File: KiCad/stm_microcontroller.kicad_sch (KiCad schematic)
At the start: 16 parts, among them SW1 SW_Push, SW2 SW_Push, U4 STM32G0B1CBTx, Y1 8Mhz

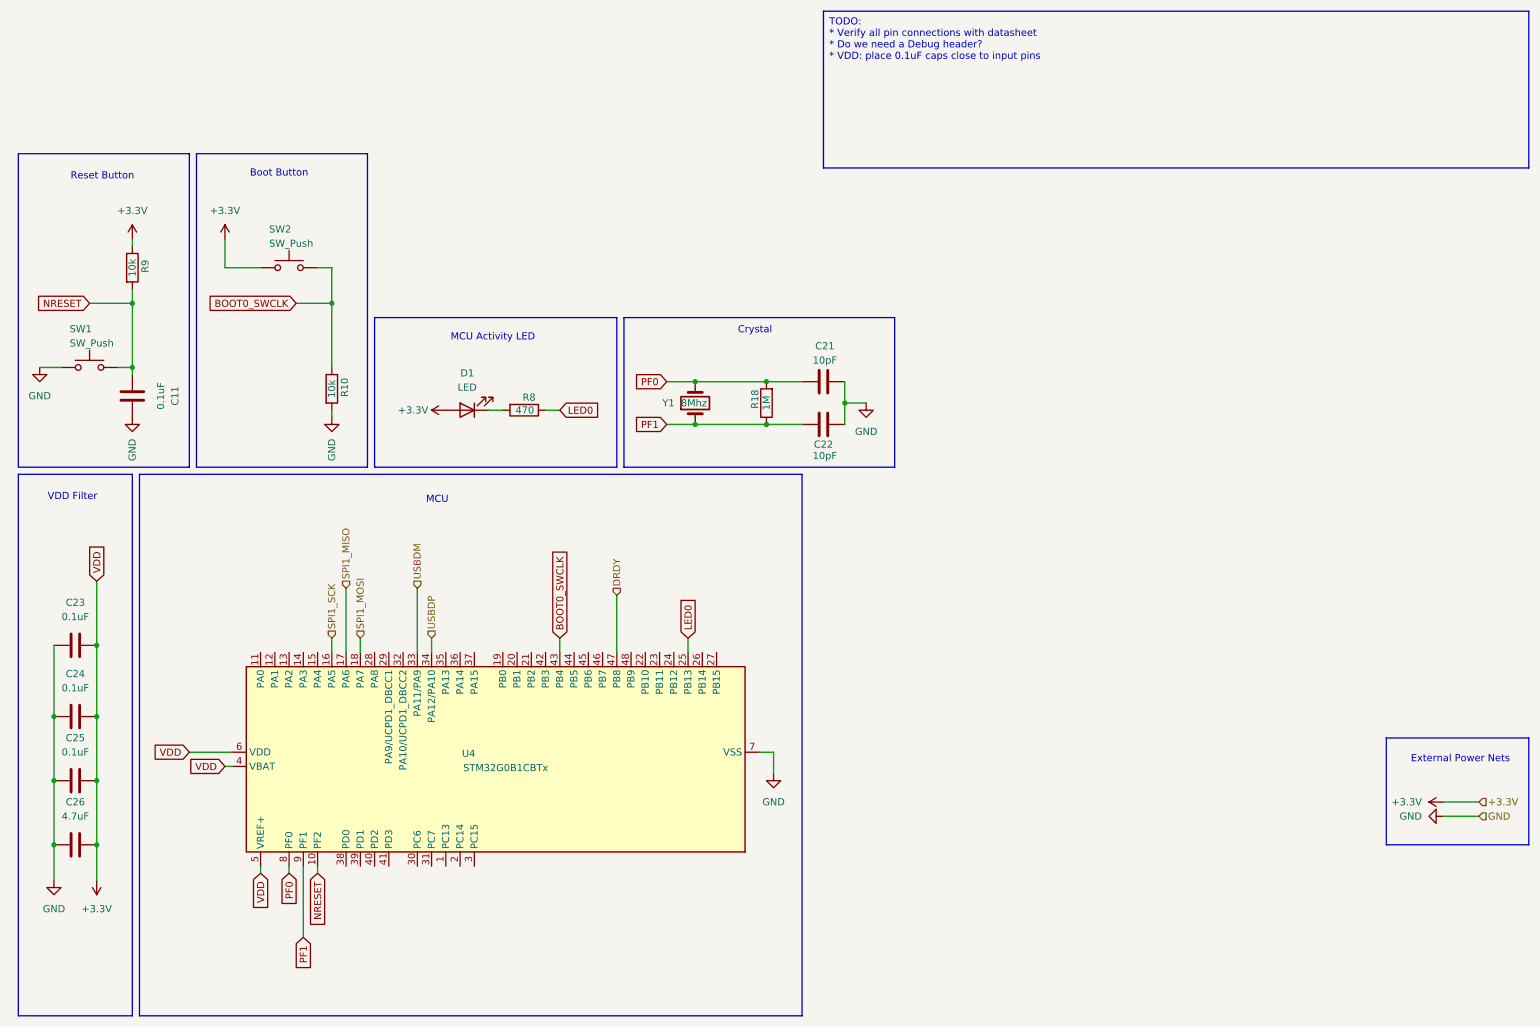
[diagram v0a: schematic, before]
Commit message: Use 12V Power
* Use 12 V Power
* Update to an F103 processor with better compatibility with Katapult
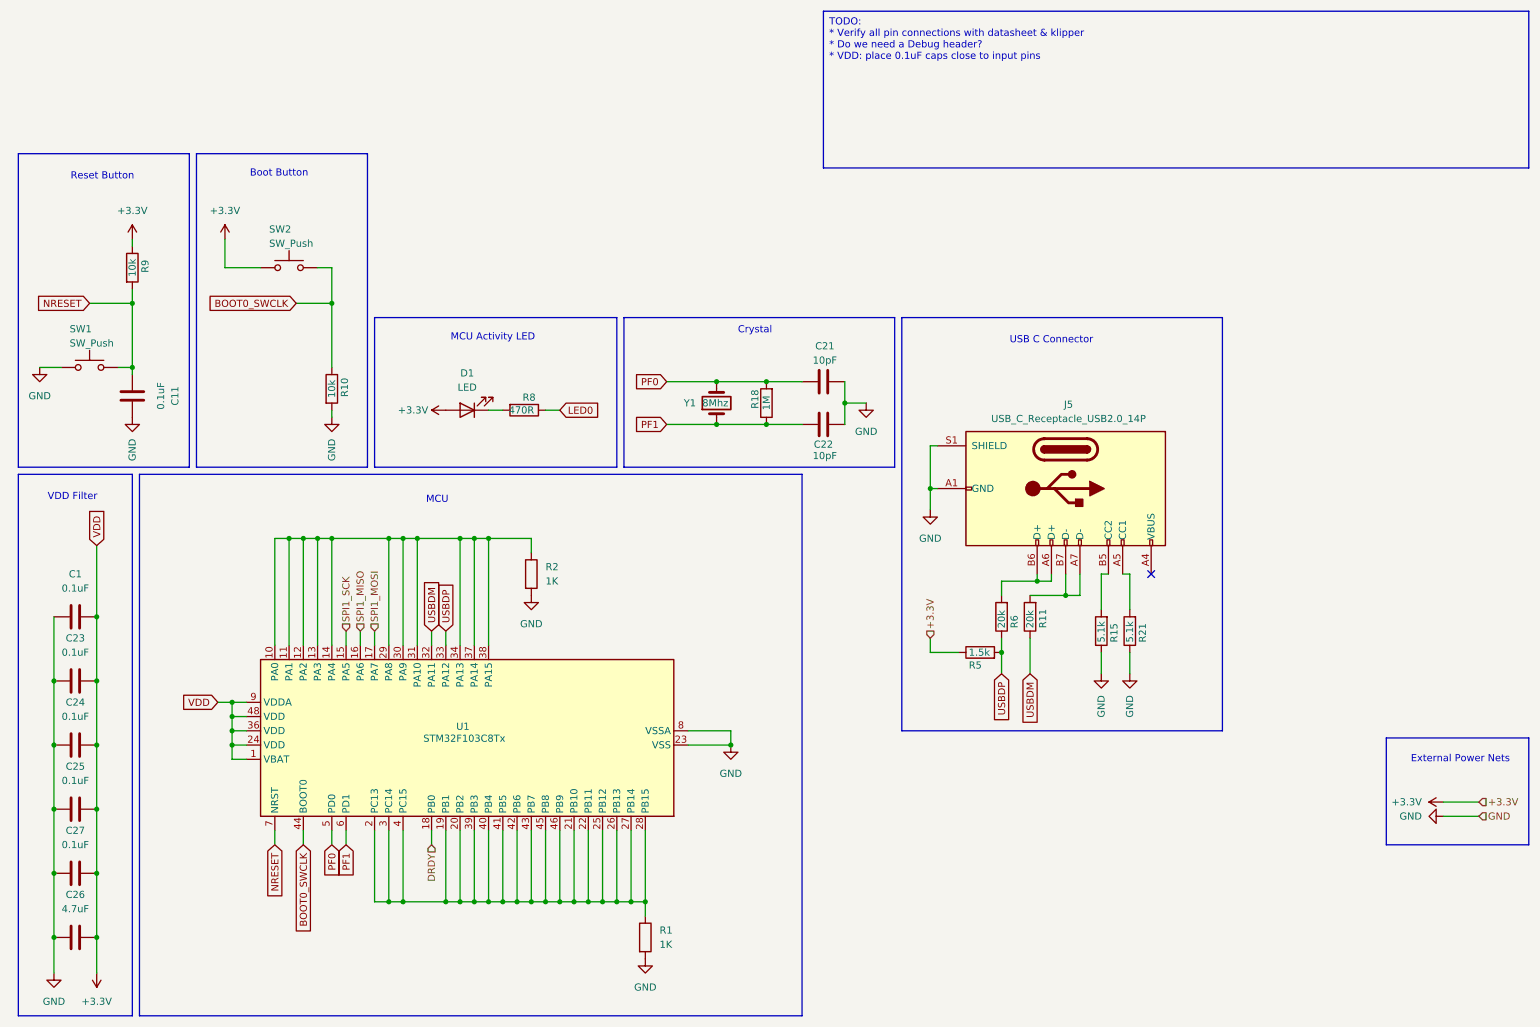
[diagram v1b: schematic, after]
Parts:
- removed U4: STM32G0B1CBTx, Package_QFP:LQFP-48_7x7mm_P0.5mm, symbol MCU_ST_STM32G0:STM32G0B1CBTx
- added C1, C27: 0.1uF, Capacitor_SMD:C_0603_1608Metric_Pad1.08x0.95mm_HandSolder, symbol Device:C
- added J5: USB_C_Receptacle_USB2.0_14P, Connector_USB:USB_C_Receptacle_GCT_USB4110, symbol Connector:USB_C_Receptacle_USB2.0_14P
- added R1, R2: 1K, Resistor_SMD:R_0603_1608Metric_Pad0.98x0.95mm_HandSolder, symbol Device:R
- added R11, R6: 20k, Resistor_SMD:R_0603_1608Metric_Pad0.98x0.95mm_HandSolder, symbol Device:R
- added R15, R21: 5.1k, Resistor_SMD:R_0603_1608Metric_Pad0.98x0.95mm_HandSolder, symbol Device:R
- added R5: 1.5k, Resistor_SMD:R_0603_1608Metric_Pad0.98x0.95mm_HandSolder, symbol Device:R
- added U1: STM32F103C8Tx, Package_QFP:LQFP-48_7x7mm_P0.5mm, symbol MCU_ST_STM32F1:STM32F103C8Tx
- C11, C21, C22, C23, C24, C25, C26: footprint (none) -> Capacitor_SMD:C_0603_1608Metric_Pad1.08x0.95mm_HandSolder
- D1: footprint (none) -> LED_SMD:LED_1206_3216Metric_Pad1.42x1.75mm_HandSolder
- R10, R18, R9: footprint (none) -> Resistor_SMD:R_0603_1608Metric_Pad0.98x0.95mm_HandSolder
- R8: value 470 -> 470R; footprint (none) -> Resistor_SMD:R_0603_1608Metric_Pad0.98x0.95mm_HandSolder
- SW1, SW2: footprint (none) -> Button_Switch_SMD:SW_Push_1P1T_NO_6x6mm_H9.5mm
- Y1: footprint (none) -> Crystal:Crystal_SMD_SeikoEpson_FA238V-4Pin_3.2x2.5mm_HandSoldering
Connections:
- net +3.3V: now also C1.2, C27.2, R5.1, U1.1 (VBAT), U1.24 (VDD), U1.36 (VDD), U1.48 (VDD), U1.9 (VDDA)
- net BOOT0_SWCLK: now also U1.44 (BOOT0)
- net DRDY: now also U1.18 (PB0)
- net GND: now also C1.1, C27.1, J5.A1 (GND), J5.A12 (GND), J5.B1 (GND), J5.B12 (GND), J5.S1 (SHIELD), R1.2, R15.1, R2.2, R21.1, U1.23 (VSS), U1.35 (VSS), U1.47 (VSS), U1.8 (VSSA)
- net NRESET: now also U1.7 (NRST)
- net PF0: now also U1.5 (PD0)
- net PF1: now also U1.6 (PD1)
- net SPI1_MISO: now also U1.16 (PA6)
- net SPI1_MOSI: now also U1.17 (PA7)
- net SPI1_SCK: now also U1.15 (PA5)
- net USBDM: now also R11.1, U1.32 (PA11)
- net USBDP: now also R5.2, R6.1, U1.33 (PA12)
- new net: R2.1, U1.10 (PA0), U1.11 (PA1), U1.12 (PA2), U1.13 (PA3), U1.14 (PA4), U1.29 (PA8), U1.30 (PA9), U1.31 (PA10), U1.34 (PA13), U1.37 (PA14), U1.38 (PA15)
- new net: J5.A4 (VBUS), J5.A9 (VBUS), J5.B4 (VBUS), J5.B9 (VBUS)
- new net: J5.A5 (CC1), R21.2
- new net: J5.A6 (D+), J5.B6 (D+), R6.2
- new net: J5.A7 (D-), J5.B7 (D-), R11.2
- new net: J5.B5 (CC2), R15.2
- new net: R1.1, U1.19 (PB1), U1.2 (PC13), U1.20 (PB2), U1.21 (PB10), U1.22 (PB11), U1.25 (PB12), U1.26 (PB13), U1.27 (PB14), U1.28 (PB15), U1.3 (PC14), U1.39 (PB3), U1.4 (PC15), U1.40 (PB4), U1.41 (PB5), U1.42 (PB6), U1.43 (PB7), U1.45 (PB8), U1.46 (PB9)
- no-connect marks 0 -> 1
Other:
- note added: "USB C Connector"
- moved on the sheet: C23, C24, C25, C26, Y1

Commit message: Update 5V Power Stage
* Update the 5V power stage based on the recommendations from TI.
* Updated standard passive footprint to 0805 hand solder configuration
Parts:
- C1, C11, C21, C22, C23, C24, C25, C26, C27: footprint Capacitor_SMD:C_0603_1608Metric_Pad1.08x0.95mm_HandSolder -> Capacitor_SMD:C_0805_2012Metric_Pad1.18x1.45mm_HandSolder
- R1, R10, R11, R15, R18, R2, R21, R5, R6, R8, R9: footprint Resistor_SMD:R_0603_1608Metric_Pad0.98x0.95mm_HandSolder -> Resistor_SMD:R_0805_2012Metric_Pad1.20x1.40mm_HandSolder
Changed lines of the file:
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@@
 			)
 		)
-		(property "Footprint" "Capacitor_SMD:C_0603_1608Metric_Pad1.08x0.95mm_HandSolder"
+		(property "Footprint" "Capacitor_SMD:C_0805_2012Metric_Pad1.18x1.45mm_HandSolder"
 			(at 27.94 143.8148 0)
 			(effects
@@
 			)
 		)
-		(property "Footprint" "Resistor_SMD:R_0603_1608Metric_Pad0.98x0.95mm_HandSolder"
+		(property "Footprint" "Resistor_SMD:R_0805_2012Metric_Pad1.20x1.40mm_HandSolder"
 			(at 103.632 114.3 90)
 			(effects
@@
 			)
 		)
-		(property "Footprint" "Resistor_SMD:R_0603_1608Metric_Pad0.98x0.95mm_HandSolder"
+		(property "Footprint" "Resistor_SMD:R_0805_2012Metric_Pad1.20x1.40mm_HandSolder"
 			(at 68.072 81.28 90)
 			(effects
@@
 			)
 		)
-		(property "Footprint" "Resistor_SMD:R_0603_1608Metric_Pad0.98x0.95mm_HandSolder"
+		(property "Footprint" "Resistor_SMD:R_0805_2012Metric_Pad1.20x1.40mm_HandSolder"
 			(at 32.512 59.69 90)
 			(effects
@@
 			)
 		)
-		(property "Footprint" "Capacitor_SMD:C_0603_1608Metric_Pad1.08x0.95mm_HandSolder"
+		(property "Footprint" "Capacitor_SMD:C_0805_2012Metric_Pad1.18x1.45mm_HandSolder"
 			(at 27.94 166.6748 0)
 			(effects
@@
 			)
 		)
-		(property "Footprint" "Resistor_SMD:R_0603_1608Metric_Pad0.98x0.95mm_HandSolder"
+		(property "Footprint" "Resistor_SMD:R_0805_2012Metric_Pad1.20x1.40mm_HandSolder"
 			(at 104.14 83.312 90)
 			(effects
@@
 			)
 		)
-		(property "Footprint" "Resistor_SMD:R_0603_1608Metric_Pad0.98x0.95mm_HandSolder"
+		(property "Footprint" "Resistor_SMD:R_0805_2012Metric_Pad1.20x1.40mm_HandSolder"
 			(at 191.008 121.92 90)
 			(effects
@@
 			)
 		)
-		(property "Footprint" "Resistor_SMD:R_0603_1608Metric_Pad0.98x0.95mm_HandSolder"
+		(property "Footprint" "Resistor_SMD:R_0805_2012Metric_Pad1.20x1.40mm_HandSolder"
 			(at 208.788 124.46 90)
 			(effects
@@
 			)
 		)
-		(property "Footprint" "Capacitor_SMD:C_0603_1608Metric_Pad1.08x0.95mm_HandSolder"
+		(property "Footprint" "Capacitor_SMD:C_0805_2012Metric_Pad1.18x1.45mm_HandSolder"
 			(at 27.94 178.1048 0)
 			(effects
@@
 			)
 		)
-		(property "Footprint" "Capacitor_SMD:C_0603_1608Metric_Pad1.08x0.95mm_HandSolder"
+		(property "Footprint" "Capacitor_SMD:C_0805_2012Metric_Pad1.18x1.45mm_HandSolder"
 			(at 153.67 88.5952 0)
 			(effects
@@
 			)
 		)
-		(property "Footprint" "Capacitor_SMD:C_0603_1608Metric_Pad1.08x0.95mm_HandSolder"
+		(property "Footprint" "Capacitor_SMD:C_0805_2012Metric_Pad1.18x1.45mm_HandSolder"
 			(at 161.29 79.0448 0)
 			(effects
@@
 			)
 		)
-		(property "Footprint" "Capacitor_SMD:C_0603_1608Metric_Pad1.08x0.95mm_HandSolder"
+		(property "Footprint" "Capacitor_SMD:C_0805_2012Metric_Pad1.18x1.45mm_HandSolder"
 			(at 27.94 155.2448 0)
 			(effects
@@
 			)
 		)
-		(property "Footprint" "Resistor_SMD:R_0603_1608Metric_Pad0.98x0.95mm_HandSolder"
+		(property "Footprint" "Resistor_SMD:R_0805_2012Metric_Pad1.20x1.40mm_HandSolder"
 			(at 149.098 83.82 90)
 			(effects
@@
 			)
 		)
-		(property "Footprint" "Resistor_SMD:R_0603_1608Metric_Pad0.98x0.95mm_HandSolder"
+		(property "Footprint" "Resistor_SMD:R_0805_2012Metric_Pad1.20x1.40mm_HandSolder"
 			(at 196.088 121.92 90)
 			(effects
@@
 			)
 		)
-		(property "Footprint" "Capacitor_SMD:C_0603_1608Metric_Pad1.08x0.95mm_HandSolder"
+		(property "Footprint" "Capacitor_SMD:C_0805_2012Metric_Pad1.18x1.45mm_HandSolder"
 			(at 27.94 132.3848 0)
 			(effects
@@
 			)
 		)
-		(property "Footprint" "Resistor_SMD:R_0603_1608Metric_Pad0.98x0.95mm_HandSolder"
+		(property "Footprint" "Resistor_SMD:R_0805_2012Metric_Pad1.20x1.40mm_HandSolder"
 			(at 185.42 130.048 90)
 			(effects
@@
 			)
 		)
-		(property "Footprint" "Resistor_SMD:R_0603_1608Metric_Pad0.98x0.95mm_HandSolder"
+		(property "Footprint" "Resistor_SMD:R_0805_2012Metric_Pad1.20x1.40mm_HandSolder"
 			(at 213.868 124.46 90)
 			(effects
@@
 			)
 		)
-		(property "Footprint" "Capacitor_SMD:C_0603_1608Metric_Pad1.08x0.95mm_HandSolder"
+		(property "Footprint" "Capacitor_SMD:C_0805_2012Metric_Pad1.18x1.45mm_HandSolder"
 			(at 27.94 120.9548 0)
 			(effects
@@
 			)
 		)
-		(property "Footprint" "Capacitor_SMD:C_0603_1608Metric_Pad1.08x0.95mm_HandSolder"
+		(property "Footprint" "Capacitor_SMD:C_0805_2012Metric_Pad1.18x1.45mm_HandSolder"
 			(at 35.2552 86.36 0)
 			(effects
@@
 			)
 		)
-		(property "Footprint" "Resistor_SMD:R_0603_1608Metric_Pad0.98x0.95mm_HandSolder"
+		(property "Footprint" "Resistor_SMD:R_0805_2012Metric_Pad1.20x1.40mm_HandSolder"
 			(at 123.952 179.07 90)
 			(effects

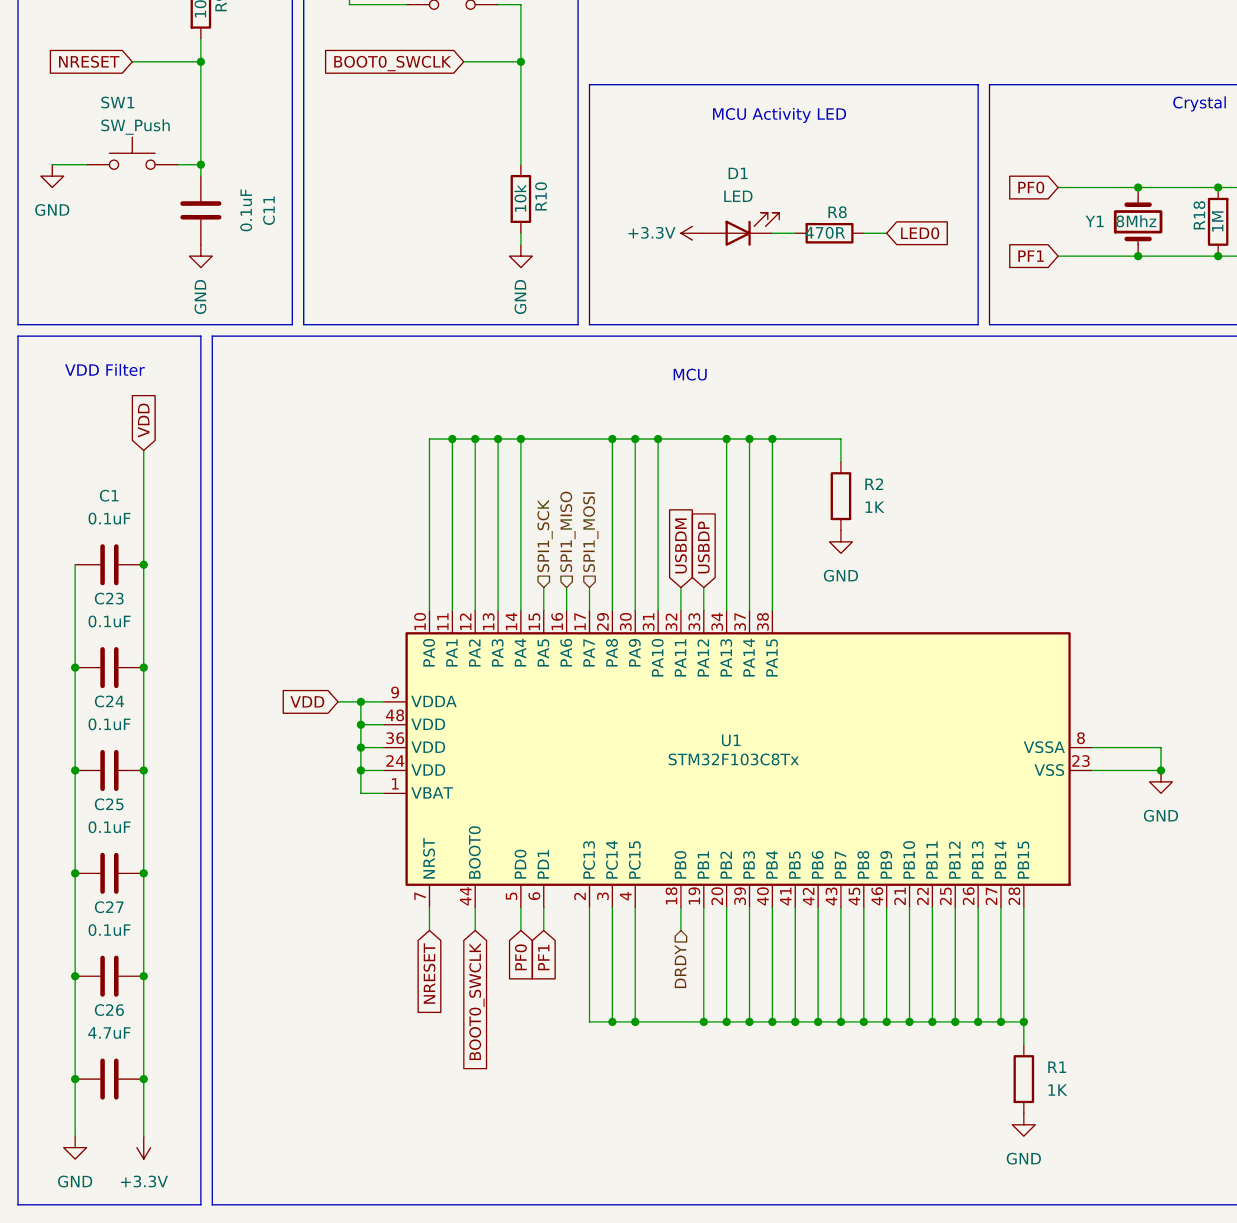
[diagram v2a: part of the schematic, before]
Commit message: Initial Routing
Taking a first pass at layout of the PCB
* load cell connectors were moved to the root schematic and placed on a bus to facilitate PCB routing
* Nets for the filters were directly connected to remove the confusion about GND verses REFN
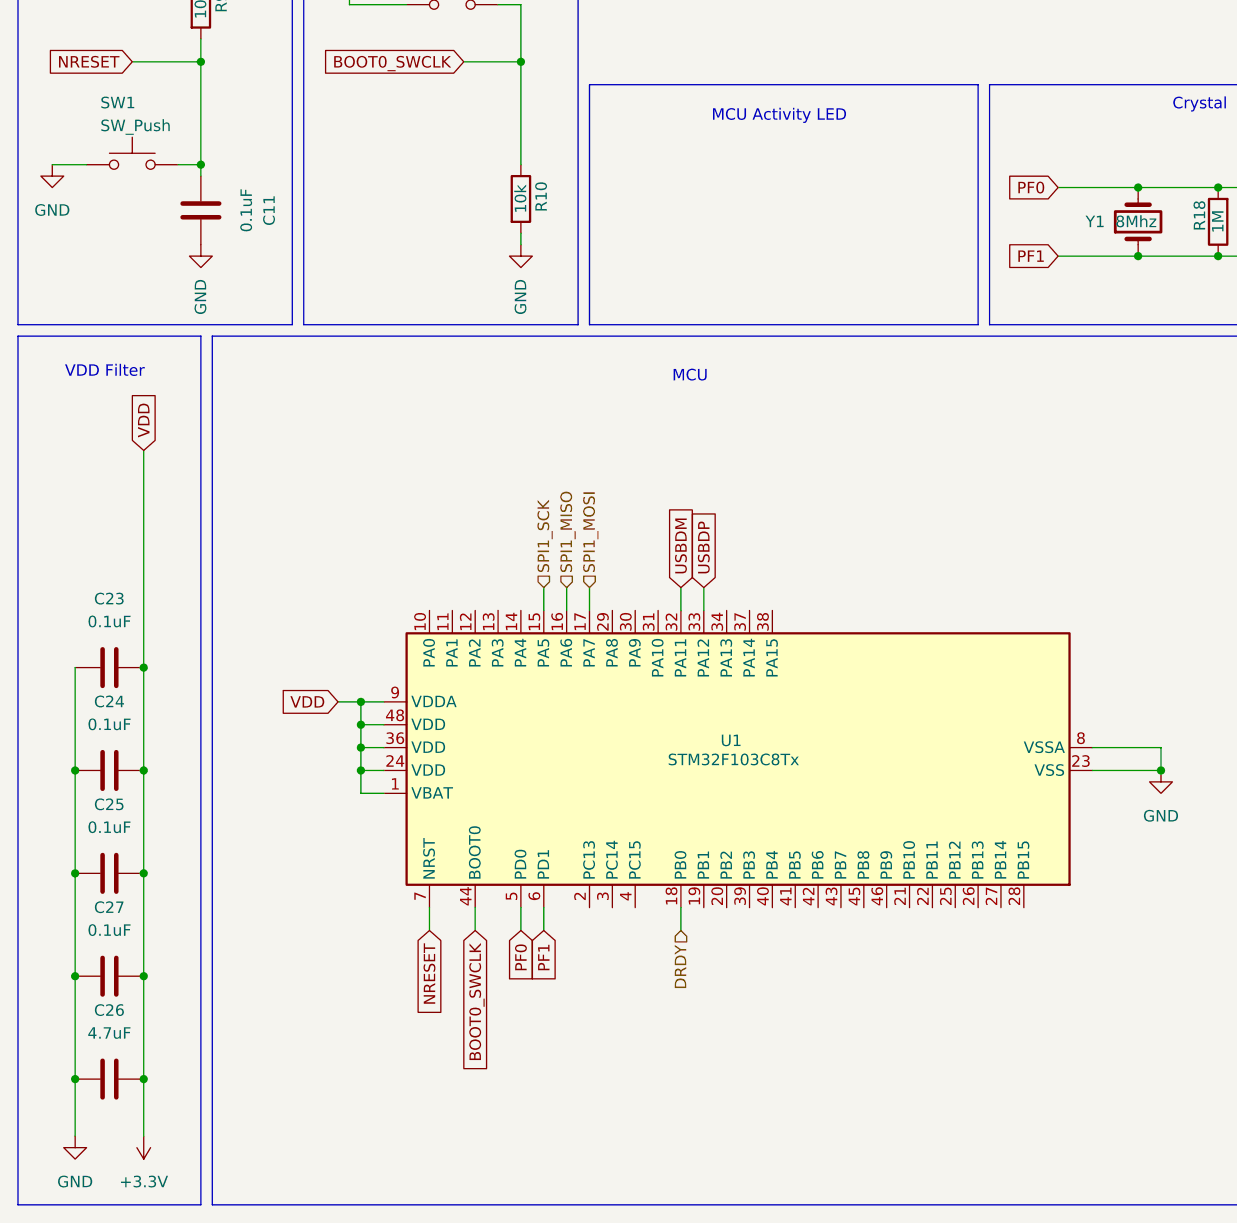
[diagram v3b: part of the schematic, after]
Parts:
- removed C1: 0.1uF, Capacitor_SMD:C_0805_2012Metric_Pad1.18x1.45mm_HandSolder, symbol Device:C
- removed D1: LED, LED_SMD:LED_1206_3216Metric_Pad1.42x1.75mm_HandSolder, symbol Device:LED
- removed R1, R2: 1K, Resistor_SMD:R_0805_2012Metric_Pad1.20x1.40mm_HandSolder, symbol Device:R
- removed R8: 470R, Resistor_SMD:R_0805_2012Metric_Pad1.20x1.40mm_HandSolder, symbol Device:R
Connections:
- now unconnected: U1.10 (PA0), U1.11 (PA1), U1.12 (PA2), U1.13 (PA3), U1.14 (PA4), U1.19 (PB1), U1.2 (PC13), U1.20 (PB2), U1.21 (PB10), U1.22 (PB11), U1.25 (PB12), U1.26 (PB13), U1.27 (PB14), U1.28 (PB15), U1.29 (PA8), U1.3 (PC14), U1.30 (PA9), U1.31 (PA10), U1.34 (PA13), U1.37 (PA14), U1.38 (PA15), U1.39 (PB3), U1.4 (PC15), U1.40 (PB4), U1.41 (PB5), U1.42 (PB6), U1.43 (PB7), U1.45 (PB8), U1.46 (PB9)
